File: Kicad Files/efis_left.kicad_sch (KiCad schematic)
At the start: 21 parts, among them J16 R_FD, J17 R_LS, J18 R_CSTR, J19 R_WPT, J20 R_VORD, J21 R_NDB, J22 R_ARPT, J51 RB_PULL, J51 RB_PUSH, J52 RB_ENC, J53 RB_hPa/inHg, J53 RVOR/ADF_1, J54 RVOR/ADF_2, J55 R_MAP_MODE, J57 R_MAP_RANGE, U1 CD74HC4067M, U2 CD74HC4067M

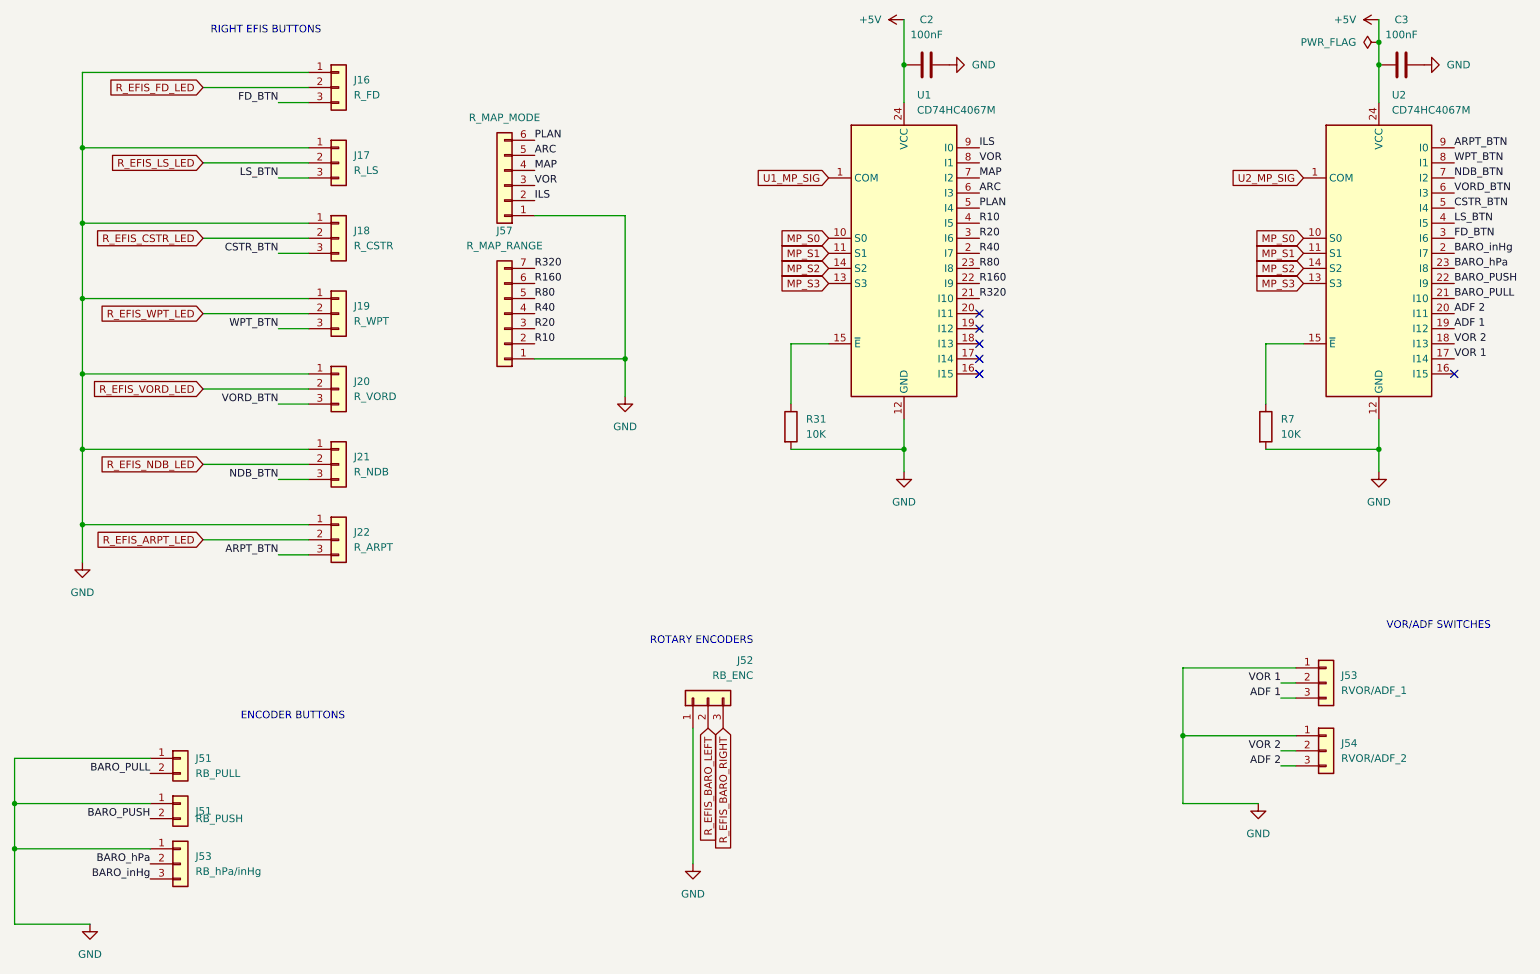
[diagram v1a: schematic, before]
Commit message: Complete rework of panels to be printed facedown. Important: change the order of the colors as Grey, White, Black, Transparent if using a Bambulab P1S/X1C ALso corrected some issue with the PCB (optional, you can print the FCU without using my pcb)
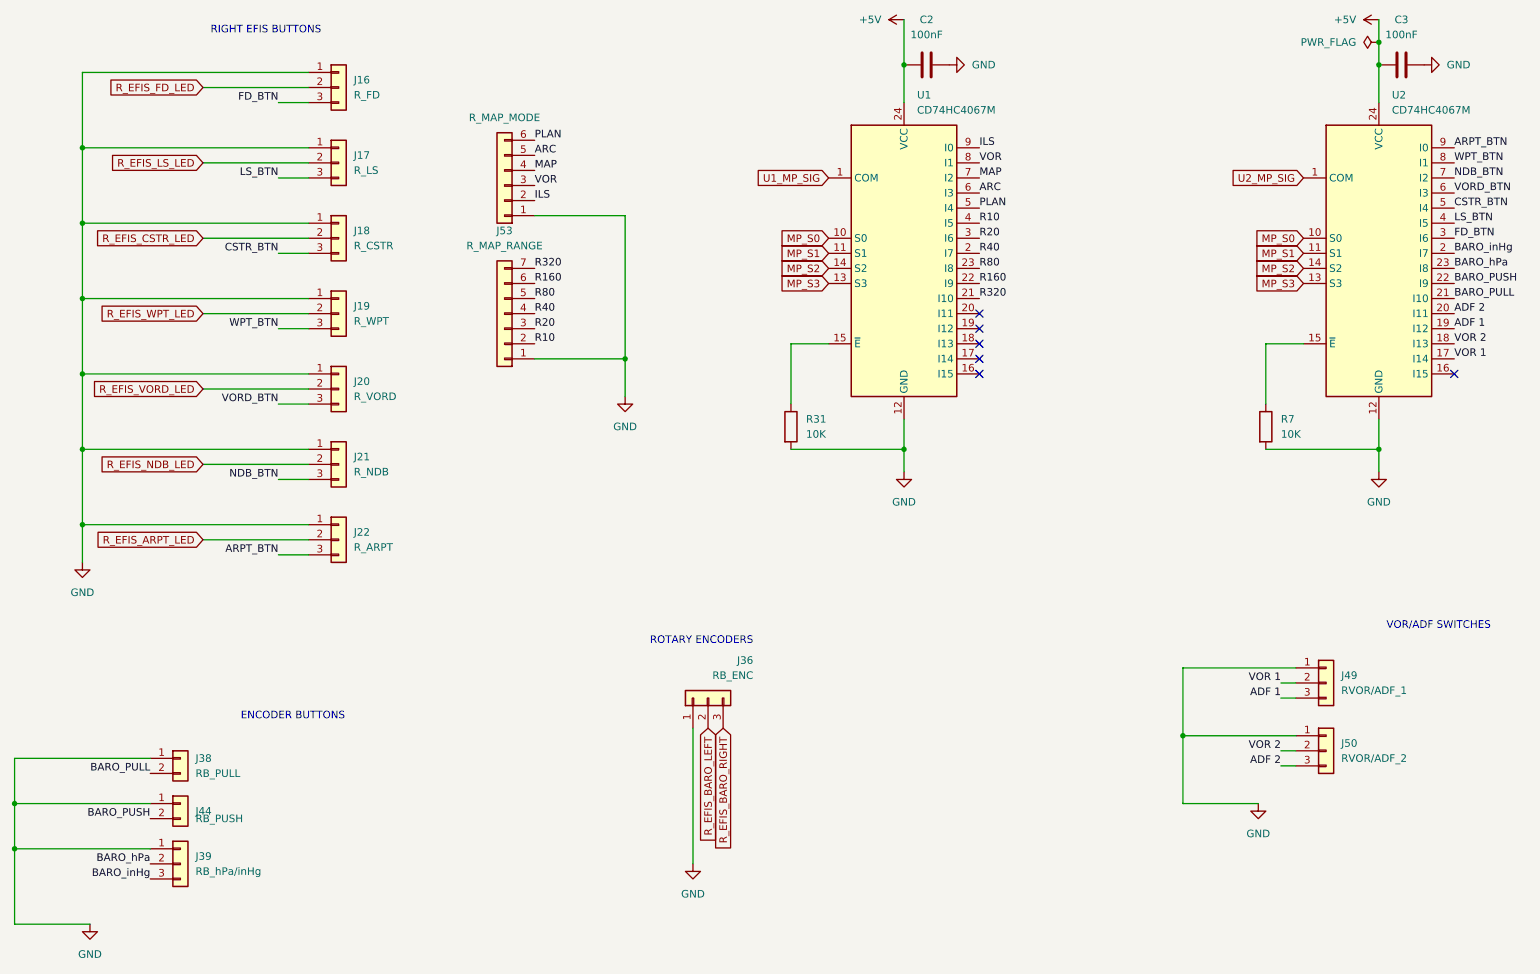
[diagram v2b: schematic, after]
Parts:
- renumbered J52 to J36, J51 to J38, J53 to J39, J51 to J44, J53 to J49, J54 to J50, J55 to J51, J57 to J53
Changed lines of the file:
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@@
 (kicad_sch
-	(version 20231120)
+	(version 20250114)
 	(generator "eeschema")
-	(generator_version "8.0")
+	(generator_version "9.0")
 	(paper "A4")
 	(title_block
@@
 		(rev "1.0")
 	)
+	(text "ENCODER BUTTONS"
+		(exclude_from_sim no)
+		(at 55.88 134.62 0)
+		(effects
+			(font
+				(size 1.27 1.27)
+			)
+			(justify left bottom)
+		)
+	)
+	(text "RIGHT EFIS BUTTONS"
+		(exclude_from_sim no)
+		(at 50.8 19.05 0)
+		(effects
+			(font
+				(size 1.27 1.27)
+			)
+			(justify left bottom)
+		)
+	)
+	(text "VOR/ADF SWITCHES"
+		(exclude_from_sim no)
+		(at 248.92 119.38 0)
+		(effects
+			(font
+				(size 1.27 1.27)
+			)
+			(justify left bottom)
+		)
+	)
+	(text "ROTARY ENCODERS"
+		(exclude_from_sim no)
+		(at 142.24 121.92 0)
+		(effects
+			(font
+				(size 1.27 1.27)
+			)
+			(justify right bottom)
+		)
+	)
 	(junction
 		(at 167.64 24.13)
@@
 		)
 	)
-	(text "ENCODER BUTTONS"
-		(exclude_from_sim no)
-		(at 55.88 134.62 0)
-		(effects
-			(font
-				(size 1.27 1.27)
-			)
-			(justify left bottom)
-		)
-	)
-	(text "RIGHT EFIS BUTTONS"
-		(exclude_from_sim no)
-		(at 50.8 19.05 0)
-		(effects
-			(font
-				(size 1.27 1.27)
-			)
-			(justify left bottom)
-		)
-	)
-	(text "VOR/ADF SWITCHES"
-		(exclude_from_sim no)
-		(at 248.92 119.38 0)
-		(effects
-			(font
-				(size 1.27 1.27)
-			)
-			(justify left bottom)
-		)
-	)
-	(text "ROTARY ENCODERS"
-		(exclude_from_sim no)
-		(at 142.24 121.92 0)
-		(effects
-			(font
-				(size 1.27 1.27)
-			)
-			(justify right bottom)
-		)
-	)
 	(label "R80"
 		(at 180.34 58.42 0)
@@
 		(dnp no)
 		(fields_autoplaced yes)
-		(property "Reference" "J51"
+		(property "Reference" "J38"
 			(at 48.26 140.9699 0)
 			(effects
@@
 		(dnp no)
 		(fields_autoplaced yes)
-		(property "Reference" "J54"
+		(property "Reference" "J50"
 			(at 241.3 138.4299 0)
 			(effects
@@
 		(on_board yes)
 		(dnp no)
-		(property "Reference" "J52"
+		(property "Reference" "J36"
 			(at 142.24 124.46 90)
 			(effects
@@
 		(dnp no)
 		(fields_autoplaced yes)
-		(property "Reference" "J55"
+		(property "Reference" "J51"
 			(at 93.98 43.18 90)
 			(effects
@@
 		(dnp no)
 		(fields_autoplaced yes)
-		(property "Reference" "J51"
+		(property "Reference" "J44"
 			(at 48.26 149.8599 0)
 			(effects
@@
 		(dnp no)
 		(fields_autoplaced yes)
-		(property "Reference" "J53"
+		(property "Reference" "J49"
 			(at 241.3 126.9999 0)
 			(effects
@@
 		(dnp no)
 		(fields_autoplaced yes)
-		(property "Reference" "J57"
+		(property "Reference" "J53"
 			(at 100.33 52.07 0)
 			(effects
@@
 		(dnp no)
 		(fields_autoplaced yes)
-		(property "Reference" "J53"
+		(property "Reference" "J39"
 			(at 48.26 157.4799 0)
 			(effects
